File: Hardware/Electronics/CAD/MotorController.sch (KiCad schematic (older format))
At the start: 14 parts, among them J1 MPE 094-1-006, J2 CONN_01X03, J3 Screw_Terminal_1x02, J5 CONN_01X04, SW2 SW_DPST_x2, U1 LD1117S33CTR, U2 MAX471, U3 TMC2130, U4 ESP-12E, U5 HiLink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

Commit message: revision1.0.0 for electrical hardware
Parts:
- added R1, R2: RND 0805 1 10K, Resistors_SMD:R_0805, symbol R
- J1: footprint Socket_Strips:Socket_Strip_Angled_1x06_Pitch2.54mm -> Pin_Headers:Pin_Header_Straight_1x06_Pitch2.54mm_SMD_Pin1Right
- J2: footprint Pin_Headers:Pin_Header_Angled_1x03_Pitch2.54mm -> Pin_Headers:Pin_Header_Straight_1x03_Pitch2.54mm_SMD_Pin1Right
- J3: footprint WAGO:WAGO_2pin -> Terminal:SolderTerminal
- J5: footprint Pin_Headers:Pin_Header_Angled_1x04_Pitch2.54mm -> Terminal:Pin_Header_SMD_Angled_2.54mm
- U5: footprint HiLink:HiLink -> HiLink:HLK-PM01
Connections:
- net CURRENT_FEEDBACK: now also R1.1; no longer U2.8 (OUT)
- net GND: now also R2.1
- net at U5.1 (AC): now also J3.2; no longer J3.1
- net at U5.2 (AC): now also J3.1; no longer J3.2
- new net: R1.2, R2.2, U2.8 (OUT)
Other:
- moved on the sheet: C1, C2, J3, J5, U1, U2, U3, U4, U5, U6

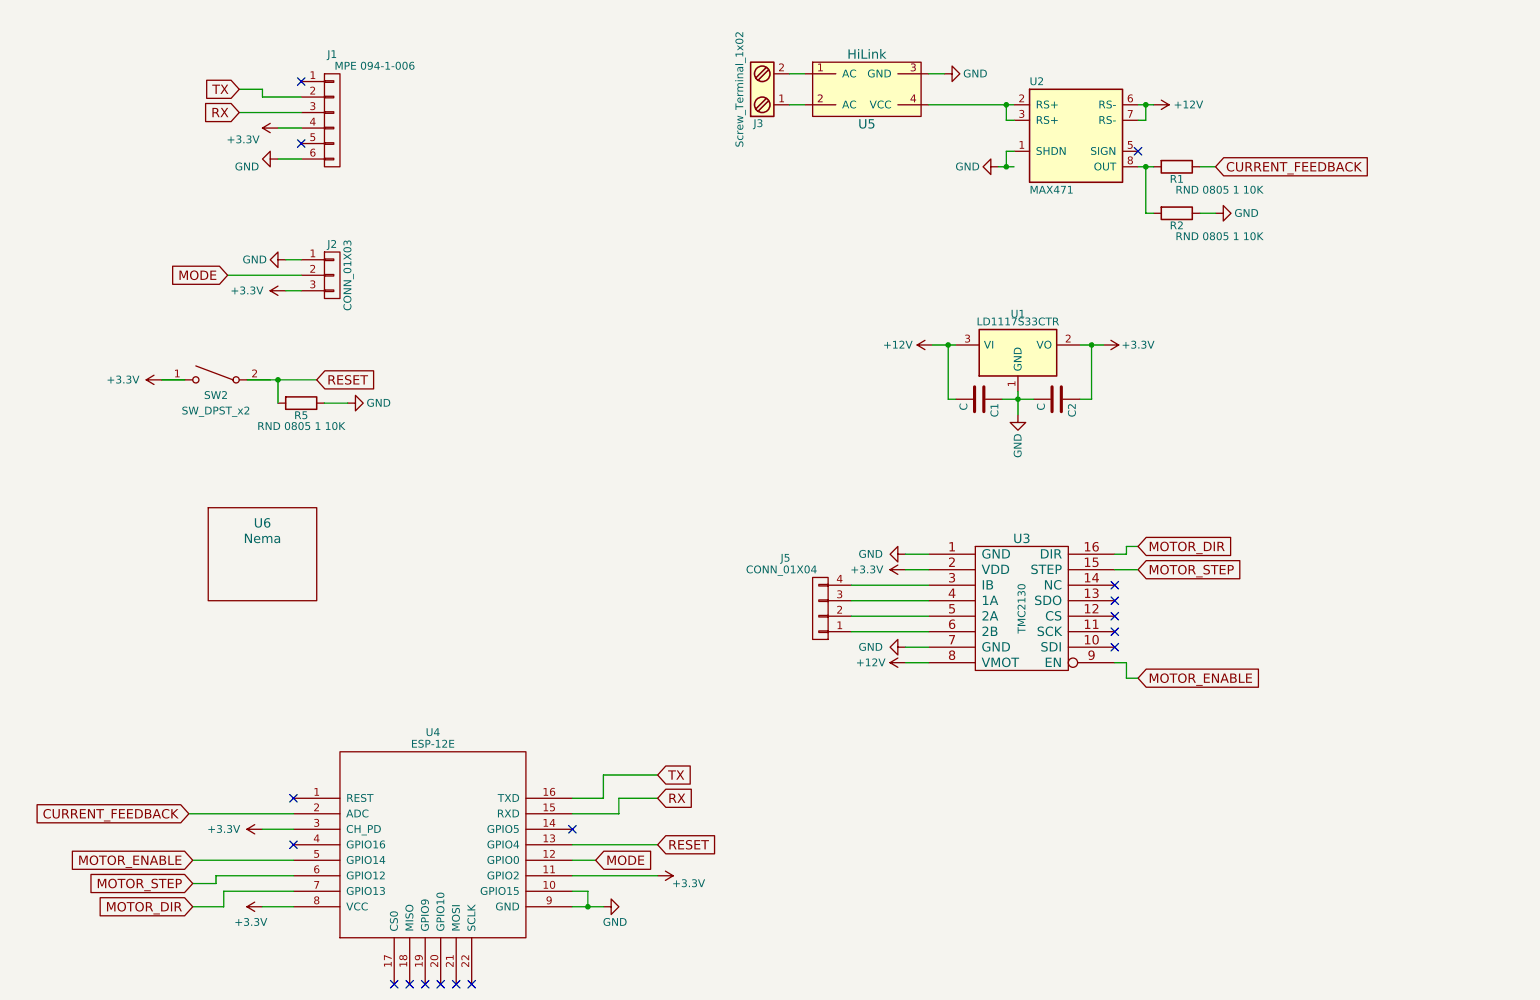
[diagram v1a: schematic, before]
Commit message: library changes
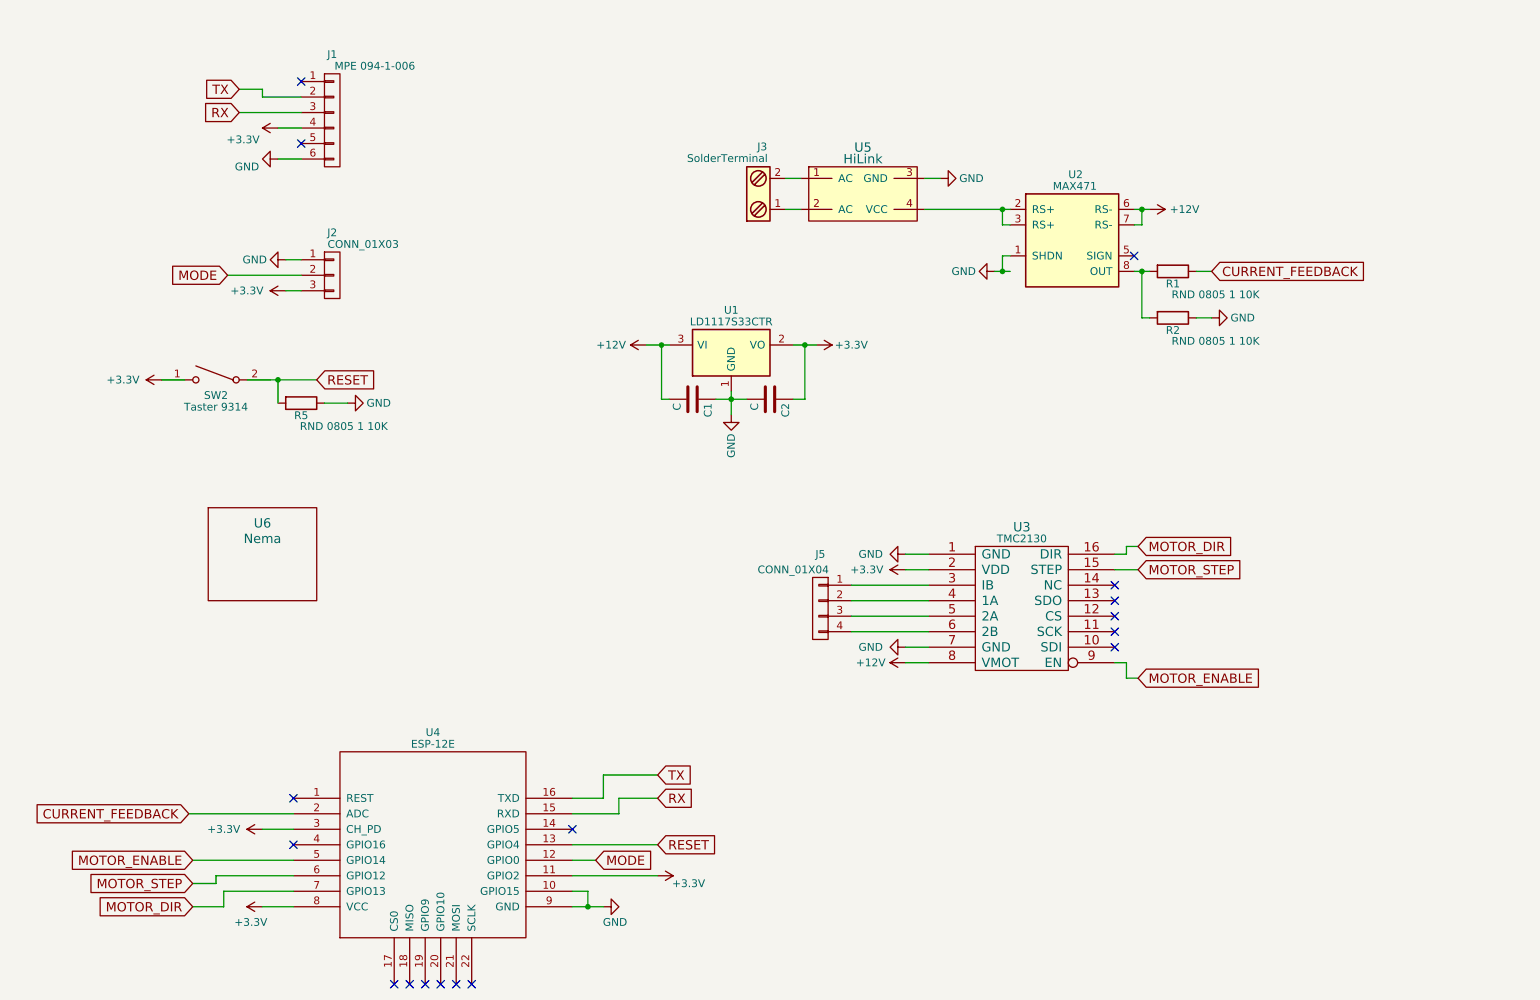
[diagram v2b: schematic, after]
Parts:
- J3: value Screw_Terminal_1x02 -> SolderTerminal
- SW2: value SW_DPST_x2 -> Taster 9314
- U2: footprint SOP:SOP-8 -> Housings_SOIC:SOIC-8_3.9x4.9mm_Pitch1.27mm
- U3: footprint StepStick:TMC2130_SMD -> StepStick:TMC2230_SMD
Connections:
- net at J5.1 (P1): now also U3.3 (IB); no longer U3.6 (2B)
- net at J5.2 (P2): now also U3.4 (1A); no longer U3.5 (2A)
- net at J5.3 (P3): now also U3.5 (2A); no longer U3.4 (1A)
- net at J5.4 (P4): now also U3.6 (2B); no longer U3.3 (IB)
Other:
- moved on the sheet: C1, C2, J3, R1, R2, U1, U2, U5

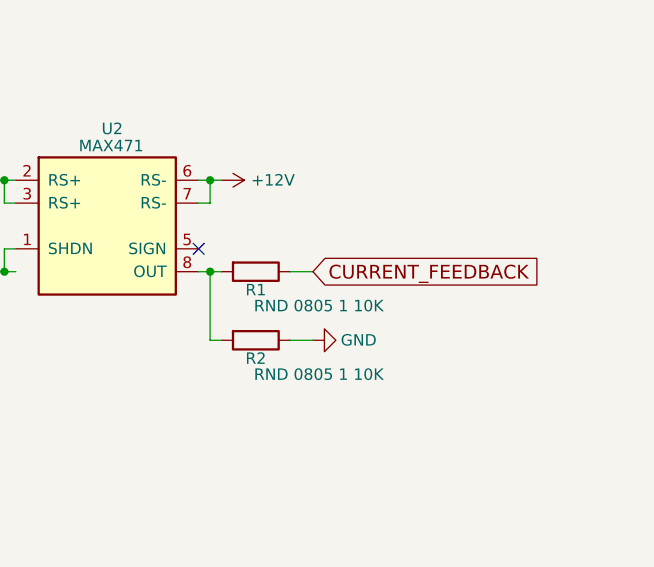
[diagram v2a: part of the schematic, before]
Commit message: bug fix current sensor
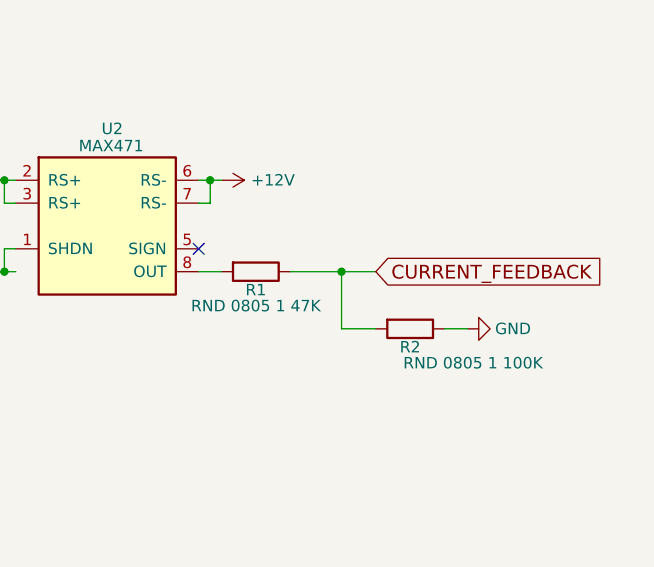
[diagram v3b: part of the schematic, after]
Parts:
- R1: value RND 0805 1 10K -> RND 0805 1 47K
- R2: value RND 0805 1 10K -> RND 0805 1 100K
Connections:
- net CURRENT_FEEDBACK: now also R2.2
- net at R1.2, U2.8 (OUT): no longer R2.2
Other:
- moved on the sheet: R2
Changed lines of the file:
@@
 	0    -1   -1   0
 $EndComp
-Text GLabel 8875 2500 2    60   Input ~ 0
+Text GLabel 9150 2500 2    60   Input ~ 0
 CURRENT_FEEDBACK
 NoConn ~ 8375 2400
@@
 Connection ~ 7525 2100
 Wire Wire Line
-	8475 2100 8375 2100
+	8375 2100 8475 2100
 Wire Wire Line
 	8375 2200 8425 2200
@@
 P 8625 2500
 F 0 "R1" V 8705 2500 50  0000 C CNN
-F 1 "RND 0805 1 10K" V 8775 2775 50  0000 C CNN
+F 1 "RND 0805 1 47K" V 8775 2500 50  0000 C CNN
 F 2 "Resistors_SMD:R_0805" V 8555 2500 50  0001 C CNN
 F 3 "" H 8625 2500 50  0001 C CNN
@@
 	0    1    1    0
 $EndComp
-Wire Wire Line
-	8775 2500 8875 2500
 $Comp
 L R R2
 U 1 1 5ACAA259
-P 8625 2800
-F 0 "R2" V 8705 2800 50  0000 C CNN
-F 1 "RND 0805 1 10K" V 8775 3075 50  0000 C CNN
-F 2 "Resistors_SMD:R_0805" V 8555 2800 50  0001 C CNN
-F 3 "" H 8625 2800 50  0001 C CNN
-	1    8625 2800
+P 9300 2750
+F 0 "R2" V 9380 2750 50  0000 C CNN
+F 1 "RND 0805 1 100K" V 9450 3025 50  0000 C CNN
+F 2 "Resistors_SMD:R_0805" V 9230 2750 50  0001 C CNN
+F 3 "" H 9300 2750 50  0001 C CNN
+	1    9300 2750
 	0    1    1    0
 $EndComp
 Wire Wire Line
-	8475 2800 8425 2800
-Wire Wire Line
-	8425 2800 8425 2500
-Connection ~ 8425 2500
+	9000 2750 9150 2750
 $Comp
 L GND #PWR021
 U 1 1 5ACAA303
-P 8875 2800
-F 0 "#PWR021" H 8875 2550 50  0001 C CNN
-F 1 "GND" V 8875 2600 50  0000 C CNN
-F 2 "" H 8875 2800 50  0001 C CNN
-F 3 "" H 8875 2800 50  0001 C CNN
-	1    8875 2800
+P 9550 2750
+F 0 "#PWR021" H 9550 2500 50  0001 C CNN
+F 1 "GND" V 9550 2550 50  0000 C CNN
+F 2 "" H 9550 2750 50  0001 C CNN
+F 3 "" H 9550 2750 50  0001 C CNN
+	1    9550 2750
 	0    -1   -1   0
 $EndComp
 Wire Wire Line
-	8775 2800 8875 2800
+	9450 2750 9550 2750
+Wire Wire Line
+	8775 2500 9150 2500
+Wire Wire Line
+	9000 2500 9000 2750
+Connection ~ 9000 2500
 $EndSCHEMATC

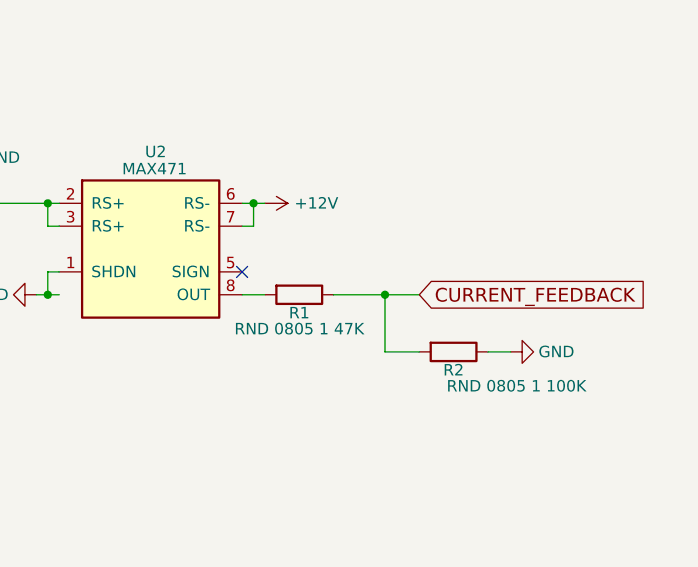
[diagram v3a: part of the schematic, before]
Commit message: MAX741 missing resistor fix
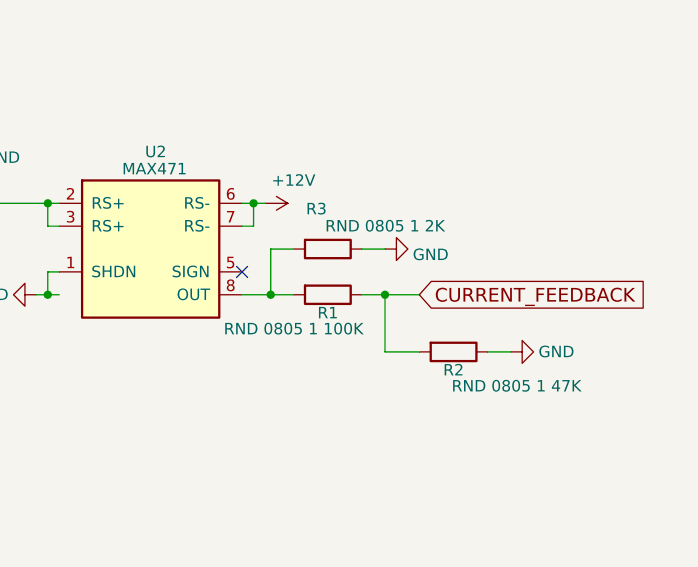
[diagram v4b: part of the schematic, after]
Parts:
- added R3: RND 0805 1 2K, Resistors_SMD:R_0805, symbol R
- R1: value RND 0805 1 47K -> RND 0805 1 100K
- R2: value RND 0805 1 100K -> RND 0805 1 47K
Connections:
- net GND: now also R3.1
- net at R1.2, U2.8 (OUT): now also R3.2
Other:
- moved on the sheet: R1
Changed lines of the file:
@@
 $EndComp
 $Comp
-L GND #PWR01
+L GND #PWR9
 U 1 1 592C2849
 P 4950 6600
-F 0 "#PWR01" H 4950 6350 50  0001 C CNN
+F 0 "#PWR9" H 4950 6350 50  0001 C CNN
 F 1 "GND" V 4850 6525 50  0000 C CNN
 F 2 "" H 4950 6600 50  0001 C CNN
@@
 $EndComp
 $Comp
-L +3.3V #PWR02
+L +3.3V #PWR3
 U 1 1 592C2C75
 P 2750 6600
-F 0 "#PWR02" H 2750 6450 50  0001 C CNN
+F 0 "#PWR3" H 2750 6450 50  0001 C CNN
 F 1 "+3.3V" V 2650 6675 50  0000 C CNN
 F 2 "" H 2750 6600 50  0001 C CNN
@@
 $EndComp
 $Comp
-L +3.3V #PWR03
+L +3.3V #PWR2
 U 1 1 592C2CAB
 P 2750 6100
-F 0 "#PWR03" H 2750 5950 50  0001 C CNN
+F 0 "#PWR2" H 2750 5950 50  0001 C CNN
 F 1 "+3.3V" V 2750 6350 50  0000 C CNN
 F 2 "" H 2750 6100 50  0001 C CNN
@@
 NoConn ~ 3900 7100
 $Comp
-L GND #PWR04
+L GND #PWR5
 U 1 1 592C460C
 P 2850 1775
-F 0 "#PWR04" H 2850 1525 50  0001 C CNN
+F 0 "#PWR5" H 2850 1525 50  0001 C CNN
 F 1 "GND" V 2900 1575 50  0000 C CNN
 F 2 "" H 2850 1775 50  0001 C CNN
@@
 MODE
 $Comp
-L GND #PWR05
+L GND #PWR6
 U 1 1 592C5F8F
 P 2900 2425
-F 0 "#PWR05" H 2900 2175 50  0001 C CNN
+F 0 "#PWR6" H 2900 2175 50  0001 C CNN
 F 1 "GND" V 2900 2225 50  0000 C CNN
 F 2 "" H 2900 2425 50  0001 C CNN
@@
 $EndComp
 $Comp
-L +3.3V #PWR06
+L +3.3V #PWR7
 U 1 1 592C600F
 P 2900 2625
-F 0 "#PWR06" H 2900 2475 50  0001 C CNN
+F 0 "#PWR7" H 2900 2475 50  0001 C CNN
 F 1 "+3.3V" V 2900 2875 50  0000 C CNN
 F 2 "" H 2900 2625 50  0001 C CNN
@@
 $EndComp
 $Comp
-L +3.3V #PWR07
+L +3.3V #PWR11
 U 1 1 595EB4E9
 P 5300 6400
-F 0 "#PWR07" H 5300 6250 50  0001 C CNN
+F 0 "#PWR11" H 5300 6250 50  0001 C CNN
 F 1 "+3.3V" V 5350 6600 50  0000 C CNN
 F 2 "" H 5300 6400 50  0001 C CNN
@@
 $EndComp
 $Comp
-L +3.3V #PWR08
+L +3.3V #PWR1
 U 1 1 599EBD49
 P 2100 3200
-F 0 "#PWR08" H 2100 3050 50  0001 C CNN
+F 0 "#PWR1" H 2100 3050 50  0001 C CNN
 F 1 "+3.3V" V 2100 3450 50  0000 C CNN
 F 2 "" H 2100 3200 50  0001 C CNN
@@
 $EndComp
 $Comp
-L GND #PWR09
+L GND #PWR8
 U 1 1 599EC69C
 P 3300 3350
-F 0 "#PWR09" H 3300 3100 50  0001 C CNN
+F 0 "#PWR8" H 3300 3100 50  0001 C CNN
 F 1 "GND" V 3300 3150 50  0000 C CNN
 F 2 "" H 3300 3350 50  0001 C CNN
@@
 RESET
 $Comp
-L +3.3V #PWR010
+L +3.3V #PWR4
 U 1 1 5A1C2463
 P 2850 1575
-F 0 "#PWR010" H 2850 1425 50  0001 C CNN
+F 0 "#PWR4" H 2850 1425 50  0001 C CNN
 F 1 "+3.3V" V 2775 1800 50  0000 C CNN
 F 2 "" H 2850 1575 50  0001 C CNN
@@
 $EndComp
 $Comp
-L +3.3V #PWR011
+L +3.3V #PWR13
 U 1 1 5A294EEF
 P 6325 2975
-F 0 "#PWR011" H 6325 2825 50  0001 C CNN
+F 0 "#PWR13" H 6325 2825 50  0001 C CNN
 F 1 "+3.3V" V 6325 3200 50  0000 C CNN
 F 2 "" H 6325 2975 50  0001 C CNN
@@
 $EndComp
 $Comp
-L +12V #PWR012
+L +12V #PWR10
 U 1 1 5A294F1E
 P 5225 2975
-F 0 "#PWR012" H 5225 2825 50  0001 C CNN
+F 0 "#PWR10" H 5225 2825 50  0001 C CNN
 F 1 "+12V" V 5225 3200 50  0000 C CNN
 F 2 "" H 5225 2975 50  0001 C CNN
@@
 $EndComp
 $Comp
-L GND #PWR013
+L GND #PWR12
 U 1 1 5A294F4D
 P 5775 3425
-F 0 "#PWR013" H 5775 3175 50  0001 C CNN
+F 0 "#PWR12" H 5775 3175 50  0001 C CNN
 F 1 "GND" V 5775 3225 50  0000 C CNN
 F 2 "" H 5775 3425 50  0001 C CNN
@@
 MOTOR_STEP
 $Comp
-L +3.3V #PWR014
+L +3.3V #PWR15
 U 1 1 5A2EB86A
 P 6900 4425
-F 0 "#PWR014" H 6900 4275 50  0001 C CNN
+F 0 "#PWR15" H 6900 4275 50  0001 C CNN
 F 1 "+3.3V" V 6900 4675 50  0000 C CNN
 F 2 "" H 6900 4425 50  0001 C CNN
@@
 $EndComp
 $Comp
-L GND #PWR015
+L GND #PWR14
 U 1 1 5A2EB8A2
 P 6900 4325
-F 0 "#PWR015" H 6900 4075 50  0001 C CNN
+F 0 "#PWR14" H 6900 4075 50  0001 C CNN
 F 1 "GND" V 6900 4100 50  0000 C CNN
 F 2 "" H 6900 4325 50  0001 C CNN
@@
 $EndComp
 $Comp
-L GND #PWR016
+L GND #PWR16
 U 1 1 5A2EC268
 P 6900 4925
-F 0 "#PWR016" H 6900 4675 50  0001 C CNN
+F 0 "#PWR16" H 6900 4675 50  0001 C CNN
 F 1 "GND" V 6900 4700 50  0000 C CNN
 F 2 "" H 6900 4925 50  0001 C CNN
@@
 $EndComp
 $Comp
-L +12V #PWR017
+L +12V #PWR17
 U 1 1 5A2EC2F3
 P 6900 5025
-F 0 "#PWR017" H 6900 4875 50  0001 C CNN
+F 0 "#PWR17" H 6900 4875 50  0001 C CNN
 F 1 "+12V" V 6900 5250 50  0000 C CNN
 F 2 "" H 6900 5025 50  0001 C CNN
@@
 $EndComp
 $Comp
-L +12V #PWR018
+L +12V #PWR20
 U 1 1 5AC69F04
 P 8475 2100
-F 0 "#PWR018" H 8475 1950 50  0001 C CNN
-F 1 "+12V" V 8475 2325 50  0000 C CNN
+F 0 "#PWR20" H 8475 1950 50  0001 C CNN
+F 1 "+12V" V 8375 2225 50  0000 C CNN
 F 2 "" H 8475 2100 50  0001 C CNN
 F 3 "" H 8475 2100 50  0001 C CNN
@@
 $EndComp
 $Comp
-L GND #PWR019
+L GND #PWR18
 U 1 1 5AC69F36
 P 7125 1900
-F 0 "#PWR019" H 7125 1650 50  0001 C CNN
+F 0 "#PWR18" H 7125 1650 50  0001 C CNN
 F 1 "GND" V 7125 1700 50  0000 C CNN
 F 2 "" H 7125 1900 50  0001 C CNN
@@
 NoConn ~ 8375 2400
 $Comp
-L GND #PWR020
+L GND #PWR19
 U 1 1 5AC6B0DF
 P 7475 2500
-F 0 "#PWR020" H 7475 2250 50  0001 C CNN
+F 0 "#PWR19" H 7475 2250 50  0001 C CNN
 F 1 "GND" V 7475 2300 50  0000 C CNN
 F 2 "" H 7475 2500 50  0001 C CNN
@@
 Wire Wire Line
 	7025 2100 7575 2100
-Wire Wire Line
-	8375 2500 8475 2500
 Wire Wire Line
 	7475 2500 7575 2500
@@
 L R R1
 U 1 1 5ACA9F3E
-P 8625 2500
-F 0 "R1" V 8705 2500 50  0000 C CNN
-F 1 "RND 0805 1 47K" V 8775 2500 50  0000 C CNN
-F 2 "Resistors_SMD:R_0805" V 8555 2500 50  0001 C CNN
-F 3 "" H 8625 2500 50  0001 C CNN
-	1    8625 2500
+P 8750 2500
+F 0 "R1" V 8830 2500 50  0000 C CNN
+F 1 "RND 0805 1 100K" V 8900 2350 50  0000 C CNN
+F 2 "Resistors_SMD:R_0805" V 8680 2500 50  0001 C CNN
+F 3 "" H 8750 2500 50  0001 C CNN
+	1    8750 2500
 	0    1    1    0
 $EndComp
@@
 P 9300 2750
 F 0 "R2" V 9380 2750 50  0000 C CNN
-F 1 "RND 0805 1 100K" V 9450 3025 50  0000 C CNN
+F 1 "RND 0805 1 47K" V 9450 3025 50  0000 C CNN
 F 2 "Resistors_SMD:R_0805" V 9230 2750 50  0001 C CNN
 F 3 "" H 9300 2750 50  0001 C CNN
@@
 	9000 2750 9150 2750
 $Comp
-L GND #PWR021
+L GND #PWR22
 U 1 1 5ACAA303
 P 9550 2750
-F 0 "#PWR021" H 9550 2500 50  0001 C CNN
+F 0 "#PWR22" H 9550 2500 50  0001 C CNN
 F 1 "GND" V 9550 2550 50  0000 C CNN
 F 2 "" H 9550 2750 50  0001 C CNN
@@
 	9450 2750 9550 2750
 Wire Wire Line
-	8775 2500 9150 2500
-Wire Wire Line
 	9000 2500 9000 2750
 Connection ~ 9000 2500
+$Comp
+L R R3
+U 1 1 5B86C0A2
+P 8750 2300
+F 0 "R3" V 8575 2250 50  0000 C CNN
+F 1 "RND 0805 1 2K" V 8650 2550 50  0000 C CNN
+F 2 "Resistors_SMD:R_0805" V 8680 2300 50  0001 C CNN
+F 3 "" H 8750 2300 50  0001 C CNN
+	1    8750 2300
+	0    1    1    0
+$EndComp
+$Comp
+L GND #PWR21
+U 1 1 5B86C312
+P 9000 2300
+F 0 "#PWR21" H 9000 2050 50  0001 C CNN
+F 1 "GND" V 8975 2100 50  0000 C CNN
+F 2 "" H 9000 2300 50  0001 C CNN
+F 3 "" H 9000 2300 50  0001 C CNN
+	1    9000 2300
+	0    -1   -1   0
+$EndComp
+Connection ~ 8500 2500
+Wire Wire Line
+	8375 2500 8600 2500
+Wire Wire Line
+	8500 2500 8500 2300
+Wire Wire Line
+	8900 2500 9150 2500
+Wire Wire Line
+	8500 2300 8600 2300
+Wire Wire Line
+	8900 2300 9000 2300
 $EndSCHEMATC
